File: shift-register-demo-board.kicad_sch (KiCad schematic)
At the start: 67 parts, among them U1 M24C64-RMN6TP, U2 W25Q128JVS, U3 74HC595, U4 SN65HVD230, U5 PCF8563T, U6 74HC595, Y1 32k768Hz

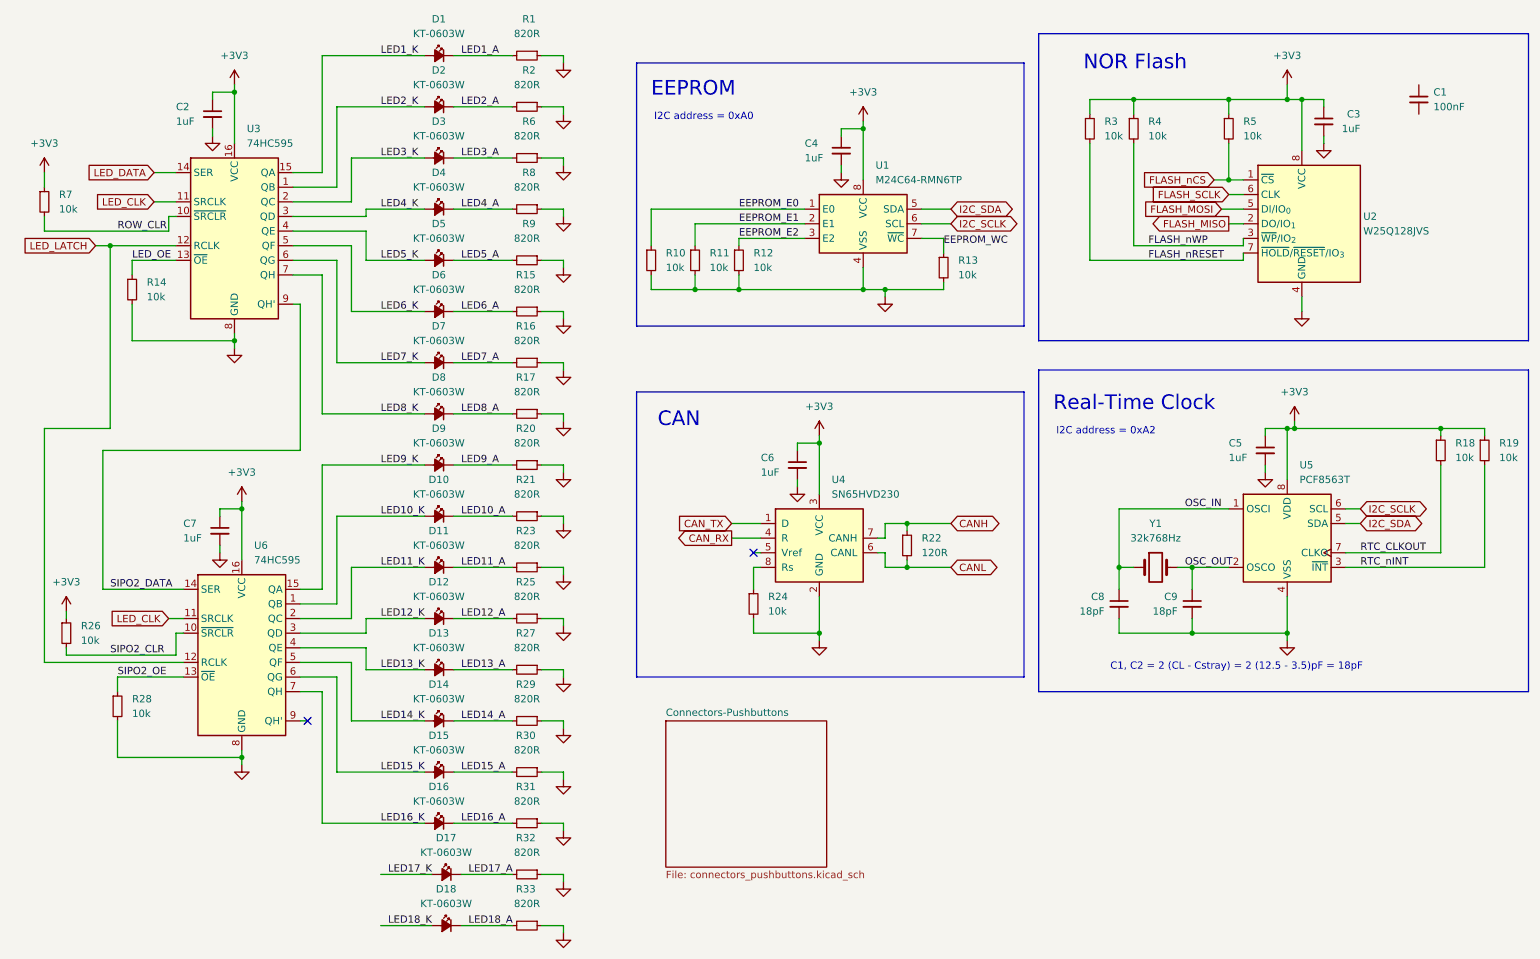
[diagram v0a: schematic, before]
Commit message: Added 2 more pushbuttons to the 74HC165 through the Schmitt trigger inverter, removed provision for unused 74HC14 inverters as a result
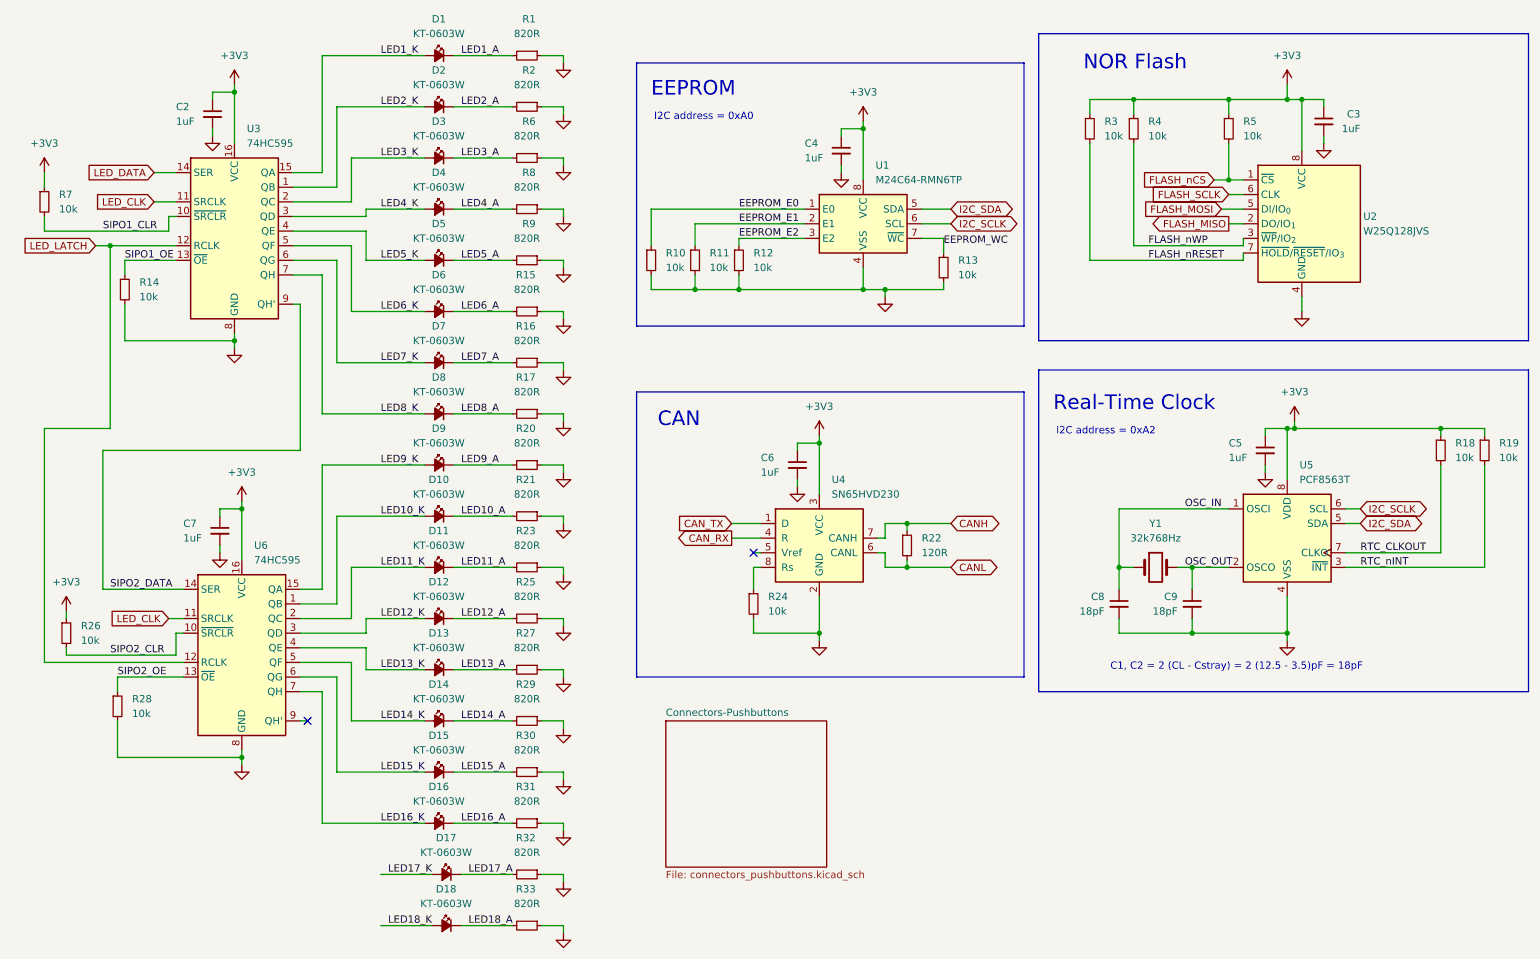
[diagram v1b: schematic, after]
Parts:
- removed C1: 100nF, Capacitor_SMD:C_0402_1005Metric, symbol Device:C_Small
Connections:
- net LED_OE renamed SIPO1_OE
- net ROW_CLR renamed SIPO1_CLR
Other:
- moved on the sheet: R14
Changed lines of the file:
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@@
 	(wire
 		(pts
+			(xy 25.4 58.42) (xy 46.99 58.42)
+		)
+		(stroke
+			(width 0)
+			(type default)
+		)
+	)
+	(wire
+		(pts
 			(xy 76.2 152.4) (xy 91.44 152.4)
 		)
@@
 	(wire
 		(pts
-			(xy 40.64 63.5) (xy 48.26 63.5)
+			(xy 39.37 63.5) (xy 48.26 63.5)
 		)
 		(stroke
@@
 	(wire
 		(pts
-			(xy 40.64 77.47) (xy 58.42 77.47)
+			(xy 39.37 77.47) (xy 58.42 77.47)
 		)
 		(stroke
@@
 	(wire
 		(pts
-			(xy 46.99 58.42) (xy 25.4 58.42)
-		)
-		(stroke
-			(width 0)
-			(type default)
-		)
-	)
-	(wire
-		(pts
 			(xy 212.09 128.27) (xy 224.79 128.27)
 		)
@@
 	(wire
 		(pts
-			(xy 40.64 63.5) (xy 40.64 66.04)
+			(xy 39.37 63.5) (xy 39.37 66.04)
 		)
 		(stroke
@@
 	(wire
 		(pts
-			(xy 40.64 71.12) (xy 40.64 77.47)
+			(xy 39.37 71.12) (xy 39.37 77.47)
 		)
 		(stroke
@@
 		)
 	)
-	(label "ROW_CLR"
-		(at 38.1 58.42 0)
+	(label "SIPO1_CLR"
+		(at 35.56 58.42 0)
 		(effects
 			(font
@@
 		)
 	)
-	(label "LED_OE"
-		(at 40.64 63.5 0)
+	(label "SIPO1_OE"
+		(at 39.37 63.5 0)
 		(effects
 			(font
@@
 	)
 	(symbol
-		(lib_id "Device:C_Small")
-		(at 264.16 35.56 0)
-		(unit 1)
-		(exclude_from_sim no)
-		(in_bom yes)
-		(on_board yes)
-		(dnp no)
-		(fields_autoplaced yes)
-		(property "Reference" "C1"
-			(at 266.7 34.2962 0)
-			(effects
-				(font
-					(size 1.27 1.27)
-				)
-				(justify left)
-			)
-		)
-		(property "Value" "100nF"
-			(at 266.7 36.8362 0)
-			(effects
-				(font
-					(size 1.27 1.27)
-				)
-				(justify left)
-			)
-		)
-		(property "Footprint" "Capacitor_SMD:C_0402_1005Metric"
-			(at 264.16 35.56 0)
-			(effects
-				(font
-					(size 1.27 1.27)
-				)
-				(hide yes)
-			)
-		)
-		(property "Datasheet" "https://mm.digikey.com/Volume0/opasdata/d220001/medias/docus/609/CL05B104KO5NNNC.pdf"
-			(at 264.16 35.56 0)
-			(effects
-				(font
-					(size 1.27 1.27)
-				)
-				(hide yes)
-			)
-		)
-		(property "Description" "Unpolarized capacitor, small symbol"
-			(at 264.16 35.56 0)
-			(effects
-				(font
-					(size 1.27 1.27)
-				)
-				(hide yes)
-			)
-		)
-		(property "Manufacturer" "Samsung Electro-Mechanics"
-			(at 264.16 35.56 0)
-			(effects
-				(font
-					(size 1.27 1.27)
-				)
-				(hide yes)
-			)
-		)
-		(property "Manufacturer Part Number" "CL05B104KO5NNNC"
-			(at 264.16 35.56 0)
-			(effects
-				(font
-					(size 1.27 1.27)
-				)
-				(hide yes)
-			)
-		)
-		(property "LCSC Part #" "C1525"
-			(at 264.16 35.56 0)
-			(effects
-				(font
-					(size 1.27 1.27)
-				)
-				(hide yes)
-			)
-		)
-		(property "MANUFACTURER" ""
-			(at 264.16 35.56 0)
-			(effects
-				(font
-					(size 1.27 1.27)
-				)
-				(hide yes)
-			)
-		)
-		(property "MP" ""
-			(at 264.16 35.56 0)
-			(effects
-				(font
-					(size 1.27 1.27)
-				)
-				(hide yes)
-			)
-		)
-		(pin "1"
-		)
-		(pin "2"
-		)
-		(instances
-			(project "shift-register-demo-board"
-				(path "/47ec96cb-c991-4fbd-b515-9767ac54263f"
-					(reference "C1")
-					(unit 1)
-				)
-			)
-		)
-	)
-	(symbol
 		(lib_name "GND_1")
 		(lib_id "power:GND")
@@
 	(symbol
 		(lib_id "Device:R_Small")
-		(at 40.64 68.58 0)
+		(at 39.37 68.58 0)
 		(unit 1)
 		(exclude_from_sim no)
@@
 		(fields_autoplaced yes)
 		(property "Reference" "R14"
-			(at 43.18 67.3099 0)
+			(at 41.91 67.3099 0)
 			(effects
 				(font
@@
 		)
 		(property "Value" "10k"
-			(at 43.18 69.8499 0)
+			(at 41.91 69.8499 0)
 			(effects
 				(font
@@
 		)
 		(property "Footprint" "Resistor_SMD:R_0603_1608Metric"
-			(at 40.64 68.58 0)
+			(at 39.37 68.58 0)
 			(effects
 				(font
@@
 		)
 		(property "Datasheet" "https://www.royalohm.com/assets/pdf/products/smd/1.pdf"
-			(at 40.64 68.58 0)
+			(at 39.37 68.58 0)
 			(effects
 				(font
@@
 		)
 		(property "Description" "Resistor, small symbol"
-			(at 40.64 68.58 0)
+			(at 39.37 68.58 0)
 			(effects
 				(font
@@
 		)
 		(property "Manufacturer" "UNI-ROYAL"
-			(at 40.64 68.58 0)
+			(at 39.37 68.58 0)
 			(effects
 				(font
@@
 		)
 		(property "Manufacturer Part Number" "0603WAF1002T5E"
-			(at 40.64 68.58 0)
+			(at 39.37 68.58 0)
 			(effects
 				(font
@@
 		)
 		(property "LCSC Part #" "C25804"
-			(at 40.64 68.58 0)
+			(at 39.37 68.58 0)
 			(effects
 				(font
@@
 		)
 		(property "MANUFACTURER" ""
-			(at 40.64 68.58 0)
+			(at 39.37 68.58 0)
 			(effects
 				(font
@@
 		)
 		(property "MP" ""
-			(at 40.64 68.58 0)
+			(at 39.37 68.58 0)
 			(effects
 				(font
@@
 		)
 		(property "Voltage" "75V"
-			(at 40.64 68.58 0)
+			(at 39.37 68.58 0)
 			(effects
 				(font
@@
 		)
 		(property "Power" "100mW"
-			(at 40.64 68.58 0)
+			(at 39.37 68.58 0)
 			(effects
 				(font
